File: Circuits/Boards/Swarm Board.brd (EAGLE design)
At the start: 63.5 x 63.5 mm, 81 parts, among them CON1 ISP(2X3), T1 NPN2N2222, T10 TEFT4300, T11 NPN2N2222, T12 NPN2N2222, T2 NPN2N2222, T3 NPN2N2222, T4 TEFT4300, T5 TEFT4300, T6 TEFT4300, T7 TEFT4300, T8 TEFT4300, T9 TEFT4300, U1 ATMEGA324P, U2 MCP73832SOT-23, U3 TB6552FN/FNG

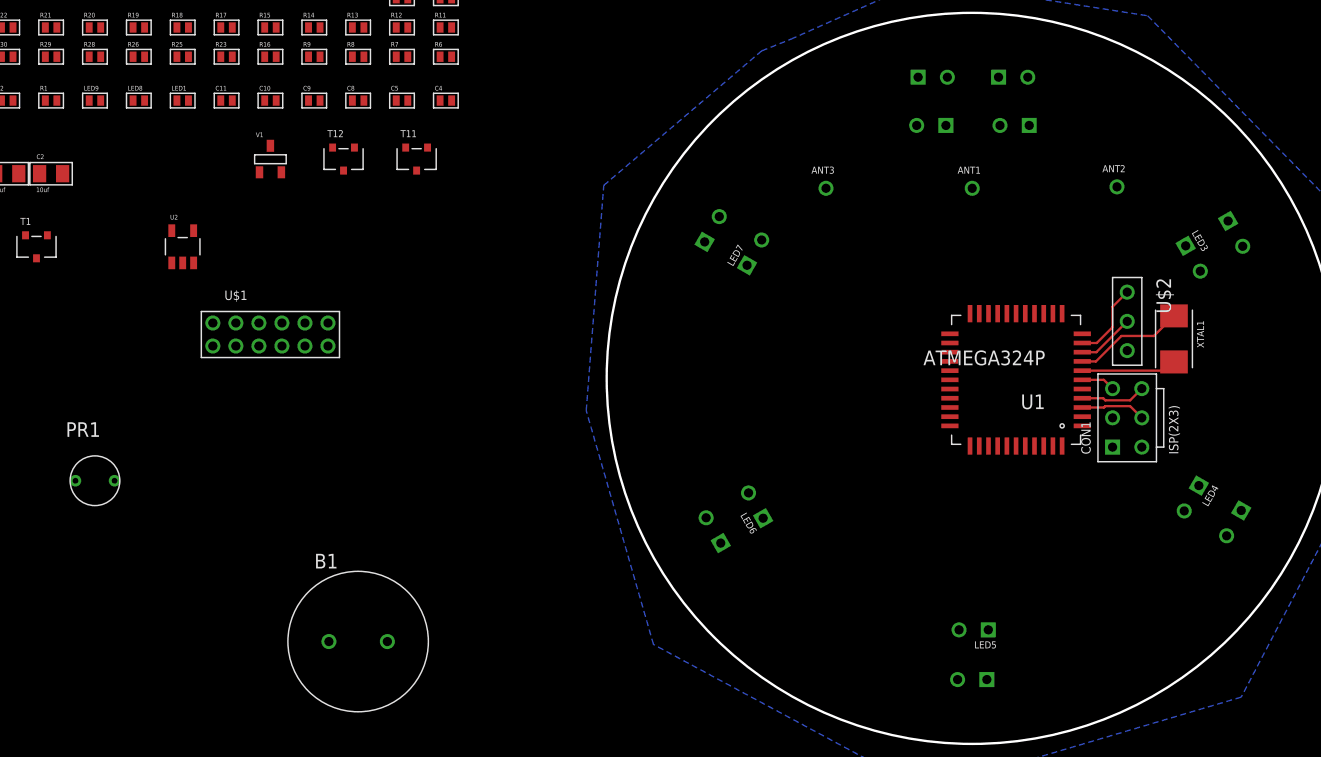
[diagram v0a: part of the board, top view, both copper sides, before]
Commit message: 
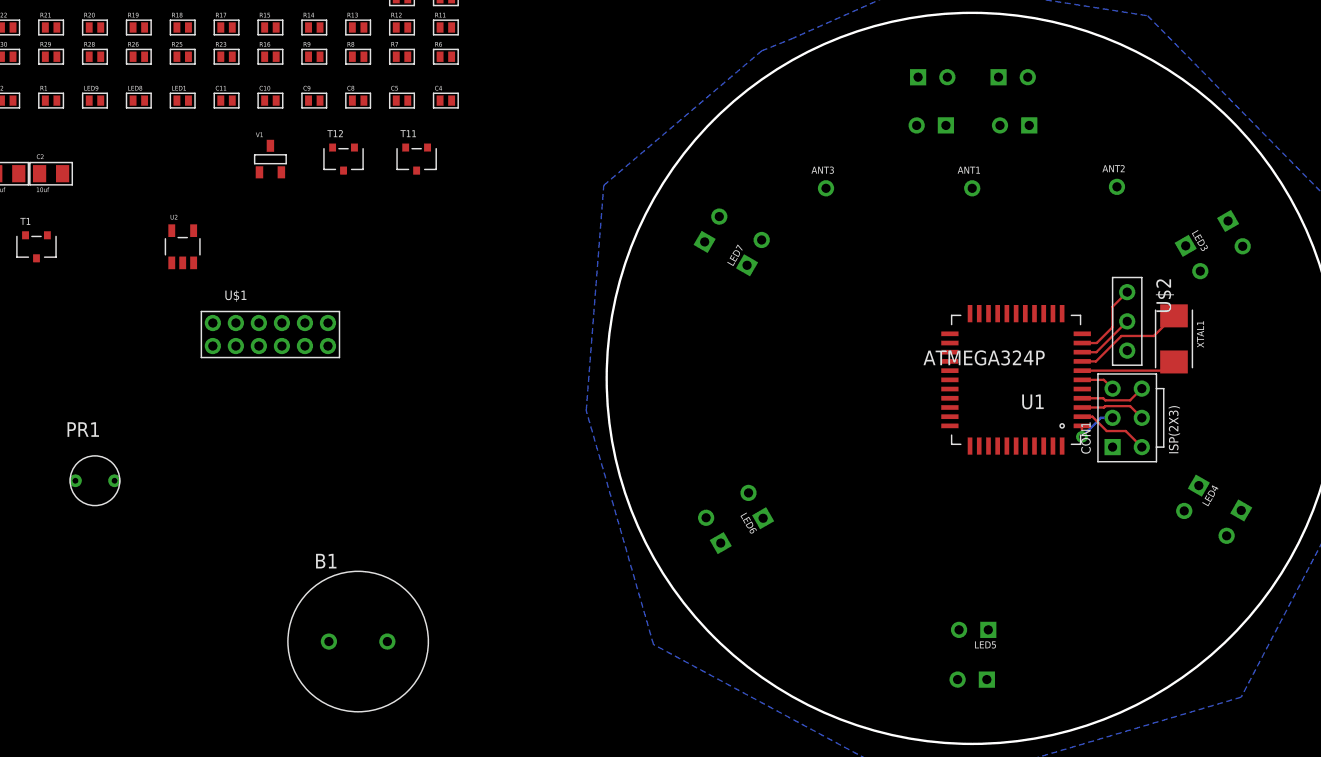
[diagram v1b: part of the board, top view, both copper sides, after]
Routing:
- net N$3: track 0.00 -> 6.27 mm
- net N$2: track 0.00 -> 4.32 mm, vias 0 -> 1
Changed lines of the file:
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@@
 </classes>
 <designrules>
-<description language="de">&lt;b&gt;EAGLE Design Rules&lt;/b&gt;
-&lt;p&gt;
-Die Standard-Design-Rules sind so gewählt, dass sie für
-die meisten Anwendungen passen. Sollte ihre Platine
-besondere Anforderungen haben, treffen Sie die erforderlichen
-Einstellungen hier und speichern die Design Rules unter
-einem neuen Namen ab.</description>
 <description language="en">&lt;b&gt;EAGLE Design Rules&lt;/b&gt;
 &lt;p&gt;
@@
 <param name="mdViaViaSameLayer" value="8mil"/>
 <param name="mnLayersViaInSmd" value="2"/>
-<param name="mdCopperDimension" value="40mil"/>
+<param name="mdCopperDimension" value="10mil"/>
 <param name="mdDrill" value="8mil"/>
 <param name="mdSmdStop" value="0mil"/>
-<param name="msWidth" value="10mil"/>
-<param name="msDrill" value="24mil"/>
+<param name="msWidth" value="8mil"/>
+<param name="msDrill" value="20mil"/>
 <param name="msMicroVia" value="9.99mm"/>
 <param name="msBlindViaRatio" value="0.5"/>
@@
 <param name="rvMicroViaOuter" value="0.25"/>
 <param name="rvMicroViaInner" value="0.25"/>
-<param name="rlMinPadTop" value="10mil"/>
+<param name="rlMinPadTop" value="12mil"/>
 <param name="rlMaxPadTop" value="20mil"/>
 <param name="rlMinPadInner" value="10mil"/>
 <param name="rlMaxPadInner" value="20mil"/>
-<param name="rlMinPadBottom" value="10mil"/>
+<param name="rlMinPadBottom" value="12mil"/>
 <param name="rlMaxPadBottom" value="20mil"/>
-<param name="rlMinViaOuter" value="8mil"/>
+<param name="rlMinViaOuter" value="10mil"/>
 <param name="rlMaxViaOuter" value="20mil"/>
-<param name="rlMinViaInner" value="8mil"/>
+<param name="rlMinViaInner" value="10mil"/>
 <param name="rlMaxViaInner" value="20mil"/>
 <param name="rlMinMicroViaOuter" value="4mil"/>
@@
 <param name="mlMinCreamFrame" value="0mil"/>
 <param name="mlMaxCreamFrame" value="0mil"/>
-<param name="mlViaStopLimit" value="0mil"/>
+<param name="mlViaStopLimit" value="25mil"/>
 <param name="srRoundness" value="0"/>
 <param name="srMinRoundness" value="0mil"/>
@@
 <contactref element="U1" pad="1"/>
 <contactref element="CON1" pad="2"/>
-<wire x1="41.31" y1="27.623" x2="43.942" y2="28.321" width="0" layer="19" extent="1-1"/>
+<wire x1="41.31" y1="27.623" x2="41.275" y2="27.588" width="0.2032" layer="1"/>
+<wire x1="41.275" y1="27.588" x2="41.275" y2="26.67" width="0.2032" layer="1"/>
+<via x="41.275" y="26.67" extent="1-16" drill="0.508"/>
+<wire x1="41.275" y1="26.67" x2="42.926" y2="28.321" width="0.2032" layer="16"/>
+<wire x1="42.926" y1="28.321" x2="43.942" y2="28.321" width="0.2032" layer="16"/>
 </signal>
 <signal name="N$3">
 <contactref element="U1" pad="2"/>
 <contactref element="CON1" pad="6"/>
-<wire x1="41.31" y1="28.423" x2="46.482" y2="25.781" width="0" layer="19" extent="1-1"/>
+<wire x1="41.31" y1="28.423" x2="42.189" y2="28.423" width="0.2032" layer="1"/>
+<wire x1="42.189" y1="28.423" x2="43.434" y2="27.178" width="0.2032" layer="1"/>
+<wire x1="43.434" y1="27.178" x2="45.085" y2="27.178" width="0.2032" layer="1"/>
+<wire x1="45.085" y1="27.178" x2="46.482" y2="25.781" width="0.2032" layer="1"/>
 </signal>
 <signal name="N$5">

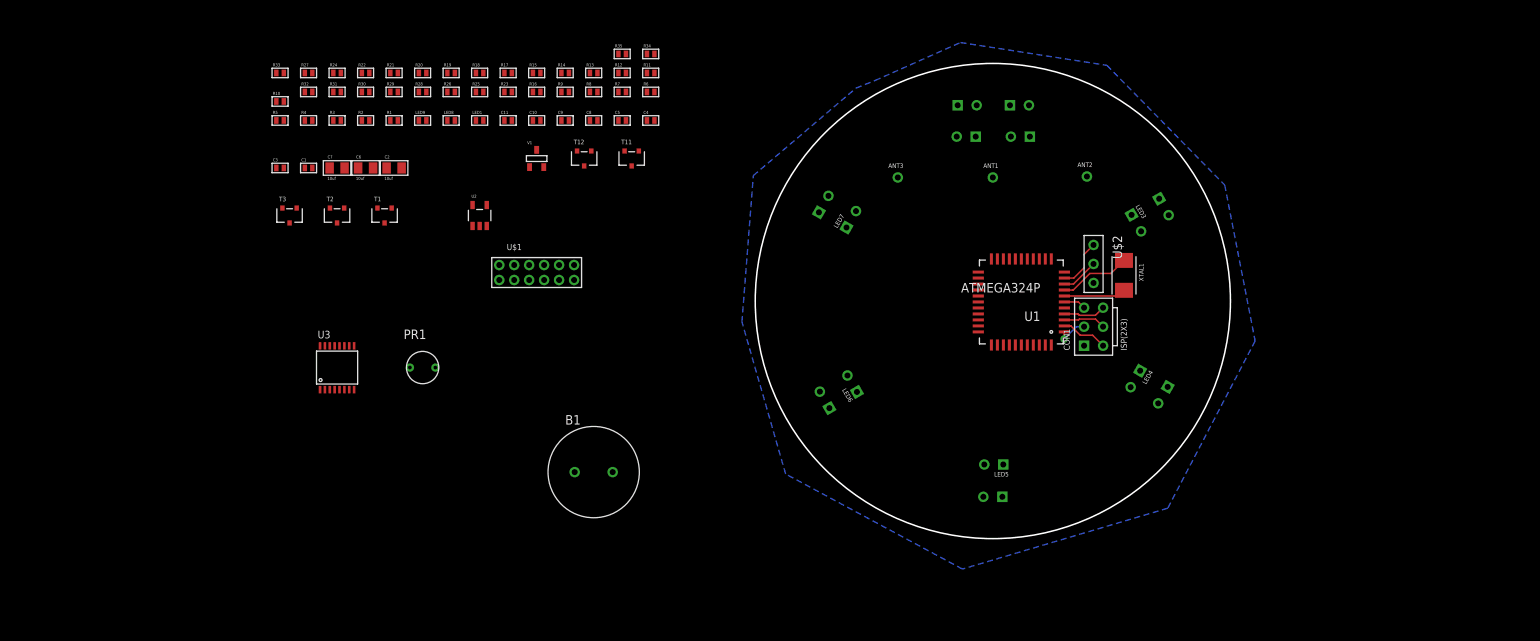
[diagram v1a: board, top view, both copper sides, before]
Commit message: 
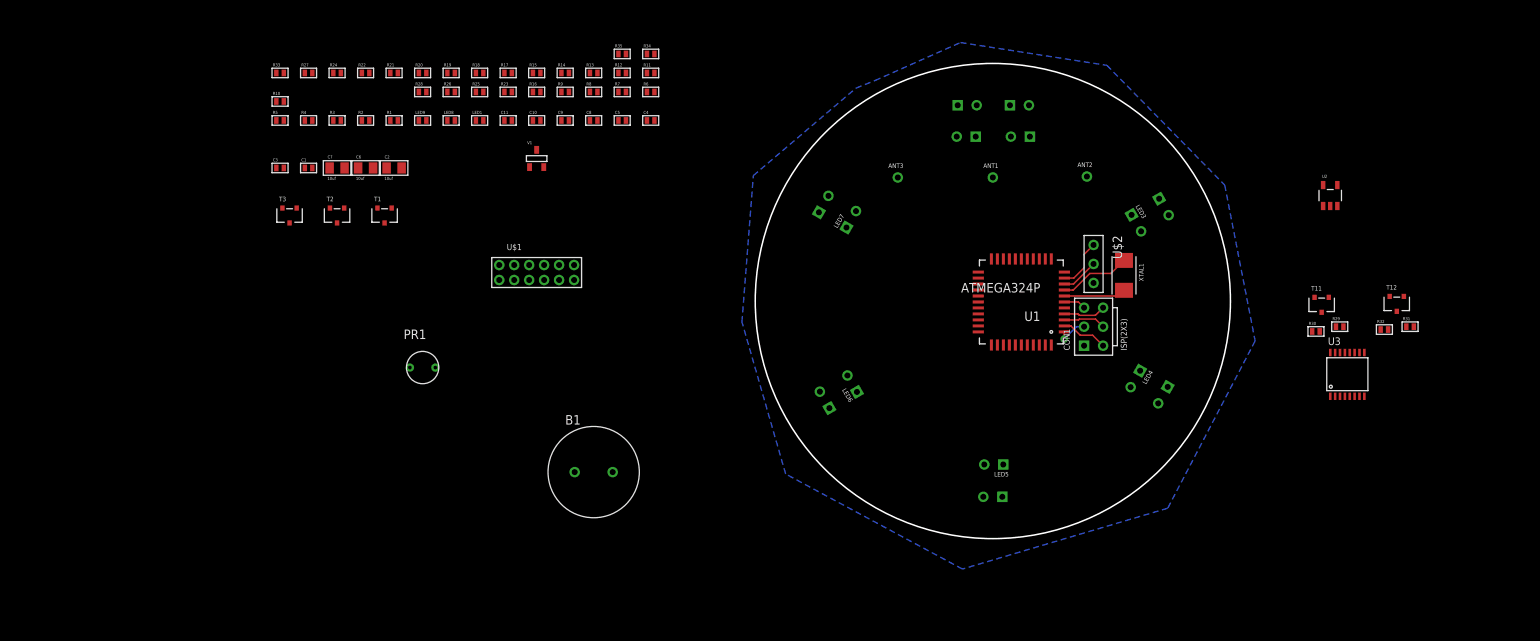
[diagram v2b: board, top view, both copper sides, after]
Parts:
- moved R32 147.2 mm to (84.1, 27.9)
- moved R31 146.8 mm to (87.5, 28.3)
- moved U3 135.0 mm to (79.1, 22.0)
- moved R30 131.0 mm to (74.9, 27.7)
- moved R29 130.2 mm to (78.1, 28.3)
- moved U2 113.7 mm to (76.8, 45.8)
- moved T12 110.3 mm to (85.7, 31.4)
- moved T11 94.3 mm to (75.7, 31.2)

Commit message: 
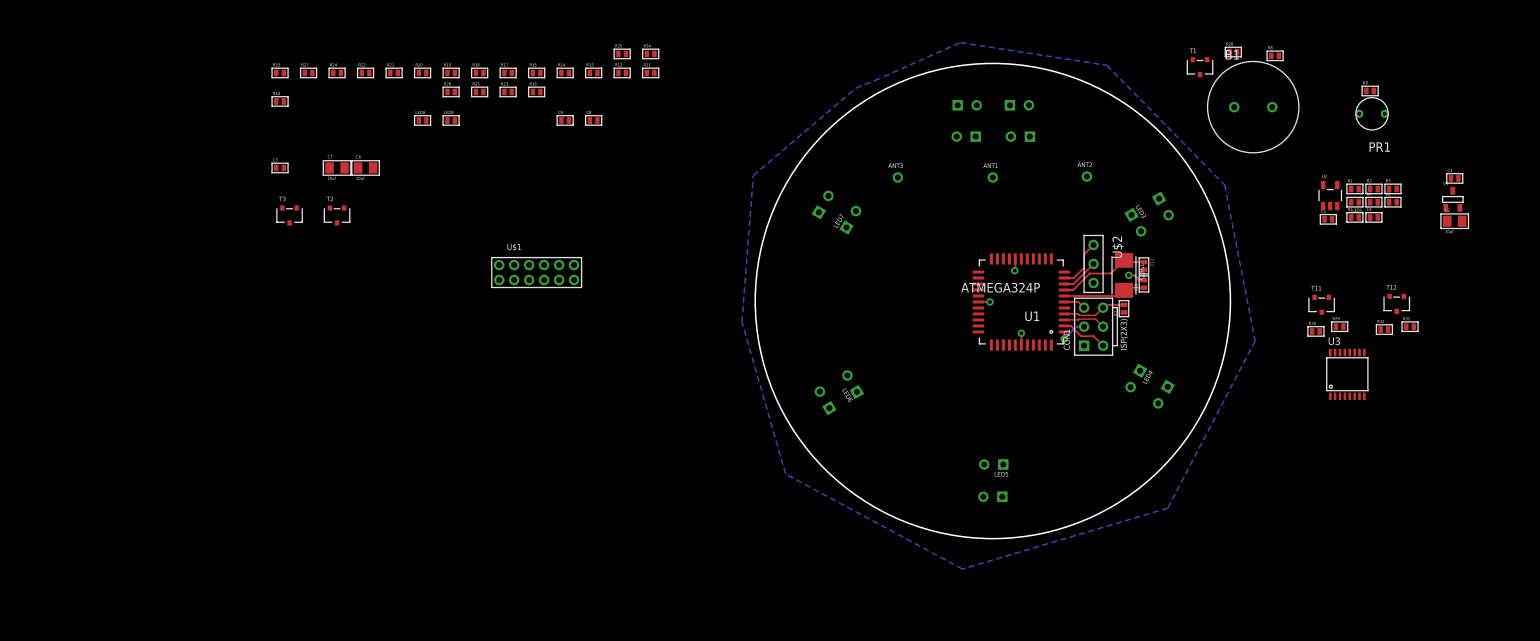
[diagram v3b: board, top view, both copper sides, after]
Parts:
- moved C1 153.2 mm to (93.5, 48.1)
- moved R5 149.0 mm to (85.2, 46.7)
- moved R4 142.8 mm to (82.7, 45.0)
- moved C2 141.9 mm to (93.5, 42.4)
- moved R3 138.9 mm to (82.7, 46.7)
- moved R2 132.5 mm to (80.1, 46.7)
- moved PR1 131.3 mm to (82.4, 56.8), turned to 180 degrees
- moved R1 129.0 mm to (80.1, 42.9)
- moved V1 122.5 mm to (93.2, 45.3)
- moved LED1 117.5 mm to (80.1, 45.0), turned to 180 degrees
- moved T1 110.8 mm to (59.4, 63.0)
- moved R28 108.5 mm to (63.9, 65.0)
- moved R9 107.6 mm to (82.2, 59.8)
- moved B1 100.7 mm to (66.5, 57.7)
- moved R6 100.3 mm to (85.2, 45.0)
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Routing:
- net GND: track 2.95 -> 11.4 mm, vias 0 -> 4
- net N$23: track 8.28 -> 11.3 mm
- net N$6: track 5.67 -> 8.62 mm
- net N$24: track 9.60 -> 12.5 mm

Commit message: 
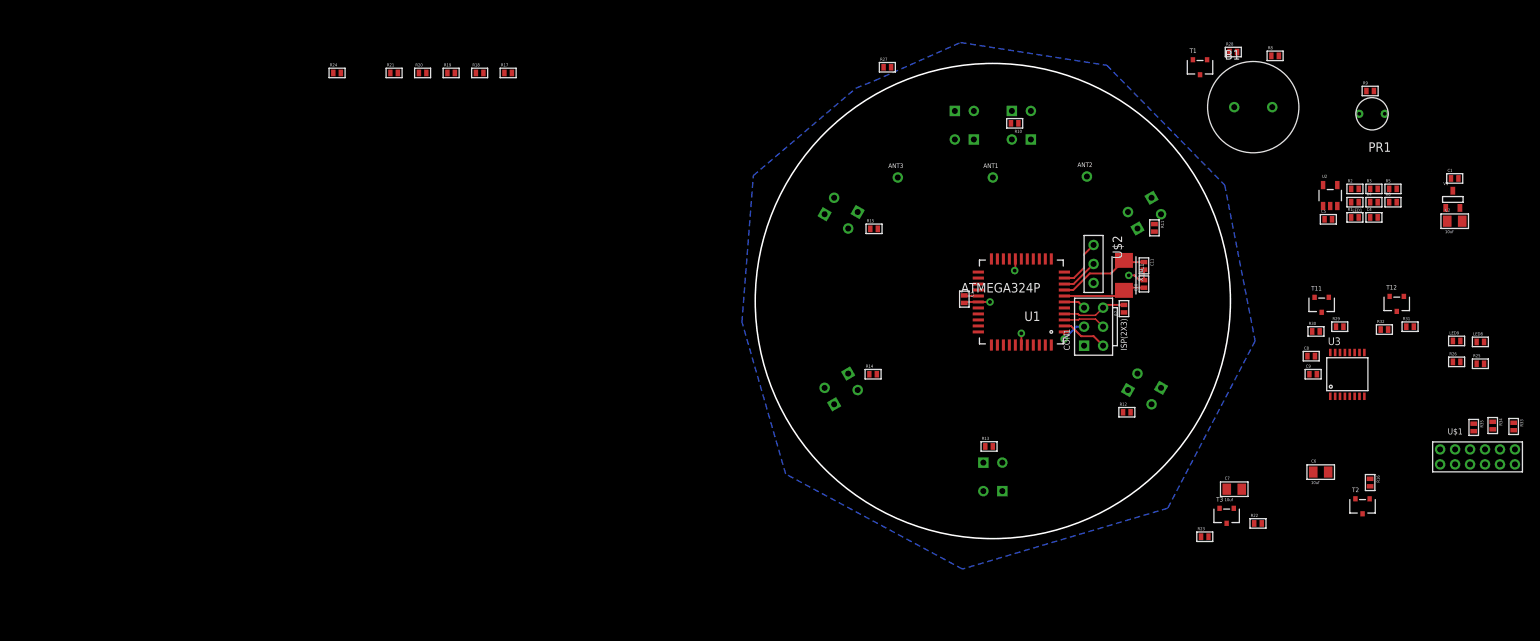
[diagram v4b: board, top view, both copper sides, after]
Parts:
- moved R33 171.5 mm to (101.3, 15.0), turned to 270 degrees
- moved T2 142.4 mm to (81.2, 4.32)
- moved LED9 141.3 mm to (93.7, 26.4)
- moved LED8 140.7 mm to (96.9, 26.3)
- moved R26 139.1 mm to (93.7, 23.6)
- moved R25 138.6 mm to (96.9, 23.4)
- moved C6 133.9 mm to (75.6, 8.89)
- moved R22 133.6 mm to (67.2, 2.03)
- moved T3 131.5 mm to (63.0, 3.05)
- moved U$1 128.1 mm to (96.5, 10.9)
- moved C7 127.3 mm to (64.0, 6.60)
- moved R35 124.3 mm to (96.0, 14.9), turned to 270 degrees
- moved R16 123.0 mm to (82.2, 7.49), turned to 270 degrees
- moved R34 123.0 mm to (98.6, 15.1), turned to 270 degrees
- moved R23 110.4 mm to (60.1, 0.25)
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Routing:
- net GND: track 11.4 -> 13.3 mm
- net +3V: track 0.00 -> 1.90 mm

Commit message: 
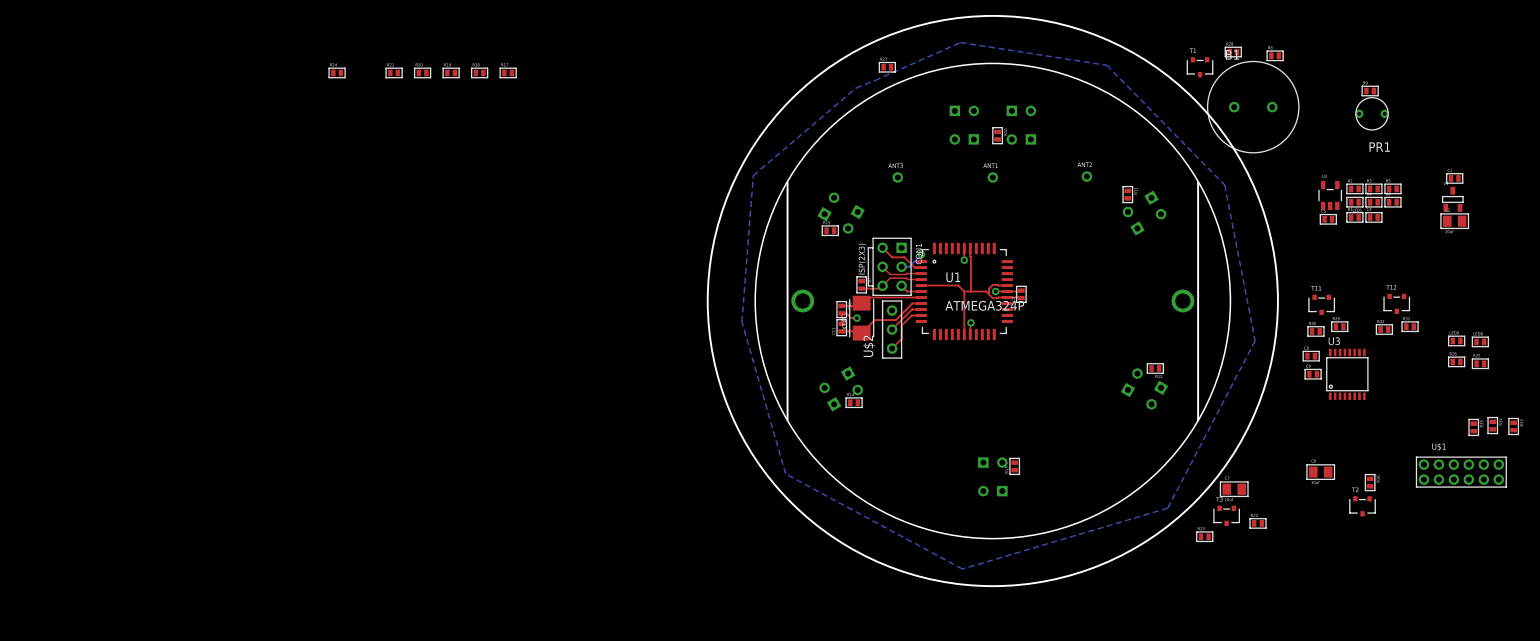
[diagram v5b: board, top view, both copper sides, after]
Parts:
- added H1, H2: MOUNTINGHOLE, Mechanical:MOUNTINGHOLE
- moved C11 41.2 mm to (11.6, 28.2), turned to 90 degrees
- moved C10 40.5 mm to (11.6, 30.6), turned to 270 degrees
- moved XTAL1 35.5 mm to (14.2, 29.5), turned to 90 degrees
- moved R7 35.2 mm to (14.2, 33.9), turned to 270 degrees
- moved U$2 28.3 mm to (18.3, 27.9), turned to 90 degrees
- moved CON1 28.1 mm to (18.3, 36.3), turned to 270 degrees
- moved U1 7.75 mm to (27.9, 33.0), turned to 0 degrees
- moved C3 7.65 mm to (35.6, 32.6), turned to 90 degrees
- moved R12 6.97 mm to (53.5, 22.7), turned to 180 degrees
- moved R15 5.85 mm to (10.0, 41.1)
- moved R11 5.69 mm to (49.8, 46.0)
- moved R14 4.58 mm to (13.2, 18.2)
- moved R13 4.34 mm to (34.7, 9.65), turned to 90 degrees
- moved U$1 2.96 mm to (94.4, 8.89)
- moved R10 2.82 mm to (32.4, 53.8), turned to 270 degrees
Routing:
- net +3V: track 1.90 -> 29.1 mm
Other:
- board size 63.5 x 63.5 mm -> 76.2 x 76.2 mm
